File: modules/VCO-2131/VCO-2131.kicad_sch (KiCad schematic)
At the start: 51 parts, among them U4 SSI2131, U5 TL074, U6 TL074, U7 TL074, U8 CD4013

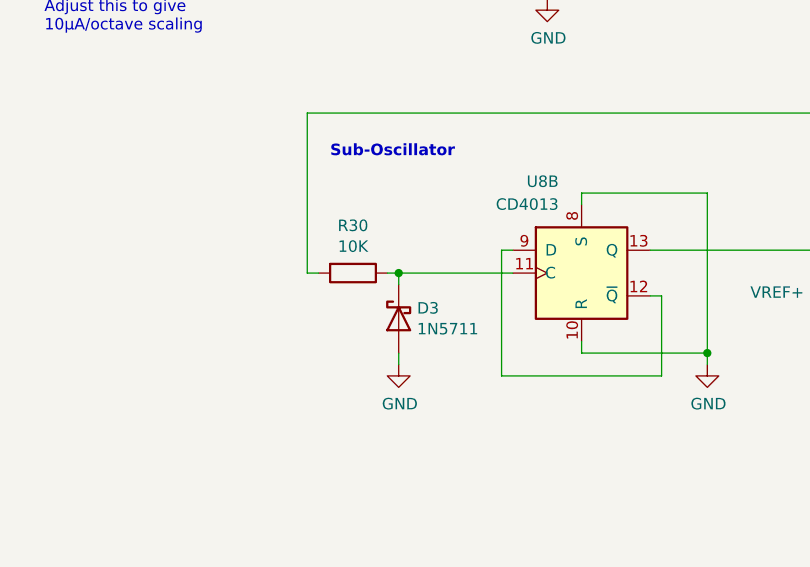
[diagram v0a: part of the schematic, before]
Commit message: VCO-2131: sub-oscillator fix
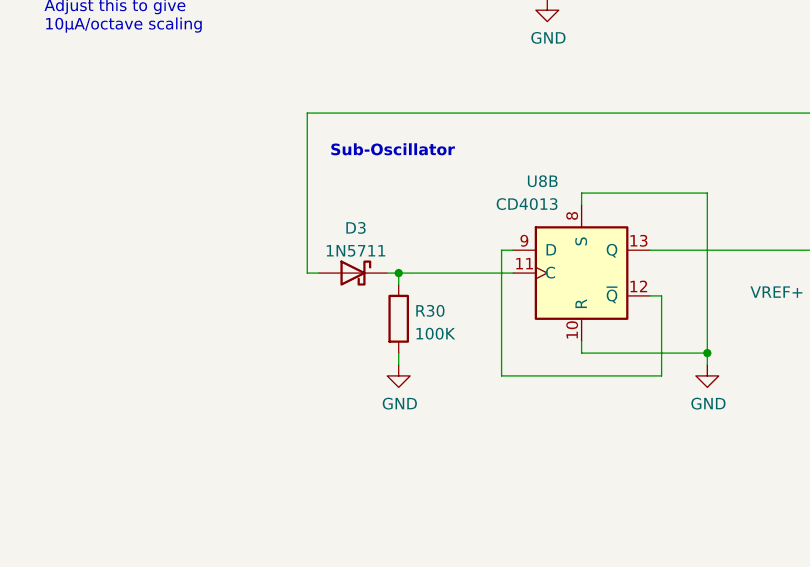
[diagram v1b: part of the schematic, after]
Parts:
- R30: value 10K -> 100K
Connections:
- net GND: now also R30.2; no longer D3.2 (A)
- net OUT-TRI: now also D3.2 (A); no longer R30.2
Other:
- moved on the sheet: D3, R30
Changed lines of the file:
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@@
   (title_block
     (title "Main - Eurorack SSI2131 VCO")
-    (date "2022-03-17")
-    (rev "1.3")
+    (date "2022-04-07")
+    (rev "1.4")
     (company "Len Popp")
     (comment 1 "Copyright © 2022 Len Popp CC BY")
@@
       (effects (font (size 1.27 1.27)) hide)
     )
+    (pin "1")
+    (pin "2")
+    (pin "3")
+    (pin "4")
+    (pin "5")
+    (pin "6")
     (pin "10")
     (pin "11")
@@
     (pin "8")
     (pin "9")
+    (pin "14")
+    (pin "7")
   )
   (symbol (lib_id "-lmp-synth:R_POT_TRIM_PCB_Vert_Bourns") (at 58.42 179.07 0) (mirror x) (unit 1)
@@
     (pin "2")
   )
-  (symbol (lib_name "R_1%_0W166_16") (lib_id "-lmp:R_1%_0W166") (at 156.21 137.16 270) (unit 1)
-    (in_bom yes) (on_board yes)
-    (property "Reference" "R30" (id 0) (at 156.21 131.9022 90))
-    (property "Value" "10K" (id 1) (at 156.21 134.2136 90))
-    (property "Footprint" "-lmp-misc:R_Axial_DIN0204_L3.6mm_D1.6mm_P7.62mm_Horizontal" (id 2) (at 156.21 135.382 90)
+  (symbol (lib_name "R_1%_0W166_16") (lib_id "-lmp:R_1%_0W166") (at 161.29 142.24 0) (unit 1)
+    (in_bom yes) (on_board yes) (fields_autoplaced)
+    (property "Reference" "R30" (id 0) (at 163.068 141.4053 0)
+      (effects (font (size 1.27 1.27)) (justify left))
+    )
+    (property "Value" "100K" (id 1) (at 163.068 143.9422 0)
+      (effects (font (size 1.27 1.27)) (justify left))
+    )
+    (property "Footprint" "-lmp-misc:R_Axial_DIN0204_L3.6mm_D1.6mm_P7.62mm_Horizontal" (id 2) (at 159.512 142.24 90)
       (effects (font (size 1.27 1.27)) hide)
     )
-    (property "Datasheet" "https://www.mouser.ca/datasheet/2/447/Yageo_LR_MFR_1-1714151.pdf" (id 3) (at 156.21 137.16 0)
+    (property "Datasheet" "https://www.mouser.ca/datasheet/2/447/Yageo_LR_MFR_1-1714151.pdf" (id 3) (at 161.29 142.24 0)
       (effects (font (size 1.27 1.27)) hide)
     )
-    (property "Value2" "1%, 1/6 W" (id 4) (at 156.21 141.478 90)
+    (property "Value2" "1%, 1/6 W" (id 4) (at 165.608 142.24 90)
       (effects (font (size 1.27 1.27)) hide)
     )
-    (property "Manufacturer" "YAGEO" (id 5) (at 156.21 137.16 0)
+    (property "Manufacturer" "YAGEO" (id 5) (at 161.29 142.24 0)
       (effects (font (size 1.27 1.27)) hide)
     )
-    (property "ManufacturerPartNum" "MFR-12FRF52-10K" (id 6) (at 156.21 137.16 0)
+    (property "ManufacturerPartNum" "MFR-12FRF52-10K" (id 6) (at 161.29 142.24 0)
       (effects (font (size 1.27 1.27)) hide)
     )
-    (property "Distributor" "Mouser" (id 7) (at 156.21 137.16 0)
+    (property "Distributor" "Mouser" (id 7) (at 161.29 142.24 0)
       (effects (font (size 1.27 1.27)) hide)
     )
-    (property "DistributorPartNum" "603-MFR-12FRF5210K" (id 8) (at 156.21 137.16 0)
+    (property "DistributorPartNum" "603-MFR-12FRF5210K" (id 8) (at 161.29 142.24 0)
       (effects (font (size 1.27 1.27)) hide)
     )
-    (property "DistributorPartLink" "https://www.mouser.ca/ProductDetail/YAGEO/MFR-12FRF52-10K?qs=%2Fha2pyFaduik%252B931GUVuOg6RLmmfil0yYFh5vxVUy4xd19JrveLWPw%3D%3D" (id 9) (at 156.21 137.16 0)
+    (property "DistributorPartLink" "https://www.mouser.ca/ProductDetail/YAGEO/MFR-12FRF52-10K?qs=%2Fha2pyFaduik%252B931GUVuOg6RLmmfil0yYFh5vxVUy4xd19JrveLWPw%3D%3D" (id 9) (at 161.29 142.24 0)
       (effects (font (size 1.27 1.27)) hide)
     )
@@
       (effects (font (size 1.27 1.27)) hide)
     )
+    (pin "1")
+    (pin "2")
+    (pin "3")
+    (pin "5")
+    (pin "6")
+    (pin "7")
     (pin "10")
     (pin "8")
     (pin "9")
+    (pin "12")
+    (pin "13")
+    (pin "14")
+    (pin "11")
+    (pin "4")
   )
   (symbol (lib_id "-lmp:CF") (at 153.67 57.15 90) (unit 1)
@@
       (effects (font (size 1.27 1.27)) hide)
     )
+    (pin "1")
+    (pin "2")
+    (pin "3")
+    (pin "5")
+    (pin "6")
+    (pin "7")
+    (pin "10")
+    (pin "8")
+    (pin "9")
     (pin "12")
     (pin "13")
     (pin "14")
+    (pin "11")
+    (pin "4")
   )
   (symbol (lib_name "R_1%_0W166_17") (lib_id "-lmp:R_1%_0W166") (at 214.63 68.58 270) (unit 1)
@@
       (effects (font (size 1.27 1.27)) hide)
     )
+    (pin "1")
+    (pin "2")
+    (pin "3")
+    (pin "5")
+    (pin "6")
+    (pin "7")
+    (pin "10")
+    (pin "8")
+    (pin "9")
     (pin "12")
     (pin "13")
     (pin "14")
+    (pin "11")
+    (pin "4")
   )
   (symbol (lib_id "-lmp-opamp:TL074") (at 91.44 39.37 0) (mirror x) (unit 4)
@@
       (effects (font (size 1.27 1.27)) hide)
     )
+    (pin "1")
+    (pin "2")
+    (pin "3")
+    (pin "5")
+    (pin "6")
+    (pin "7")
+    (pin "10")
+    (pin "8")
+    (pin "9")
     (pin "12")
     (pin "13")
     (pin "14")
+    (pin "11")
+    (pin "4")
   )
   (symbol (lib_name "R_1%_0W166_1") (lib_id "-lmp:R_1%_0W166") (at 72.39 36.83 270) (unit 1)
@@
       (effects (font (size 1.27 1.27)) hide)
     )
+    (pin "1")
+    (pin "2")
+    (pin "3")
     (pin "5")
     (pin "6")
     (pin "7")
+    (pin "10")
+    (pin "8")
+    (pin "9")
+    (pin "12")
+    (pin "13")
+    (pin "14")
+    (pin "11")
+    (pin "4")
   )
   (symbol (lib_name "R_1%_0W166_6") (lib_id "-lmp:R_1%_0W166") (at 83.82 130.81 270) (unit 1)
@@
     (pin "2")
     (pin "3")
+    (pin "5")
+    (pin "6")
+    (pin "7")
+    (pin "10")
+    (pin "8")
+    (pin "9")
+    (pin "12")
+    (pin "13")
+    (pin "14")
+    (pin "11")
+    (pin "4")
   )
   (symbol (lib_id "-lmp-opamp:TL074") (at 228.6 100.33 0) (mirror x) (unit 2)
@@
       (effects (font (size 1.27 1.27)) hide)
     )
+    (pin "1")
+    (pin "2")
+    (pin "3")
     (pin "5")
     (pin "6")
     (pin "7")
+    (pin "10")
+    (pin "8")
+    (pin "9")
+    (pin "12")
+    (pin "13")
+    (pin "14")
+    (pin "11")
+    (pin "4")
   )
   (symbol (lib_id "-lmp-opamp:TL074") (at 67.31 92.71 0) (mirror x) (unit 3)
@@
       (effects (font (size 1.27 1.27)) hide)
     )
+    (pin "1")
+    (pin "2")
+    (pin "3")
+    (pin "5")
+    (pin "6")
+    (pin "7")
     (pin "10")
     (pin "8")
     (pin "9")
+    (pin "12")
+    (pin "13")
+    (pin "14")
+    (pin "11")
+    (pin "4")
   )
   (symbol (lib_id "-lmp-opamp:TL074") (at 228.6 36.83 0) (mirror x) (unit 3)
@@
       (effects (font (size 1.27 1.27)) hide)
     )
+    (pin "1")
+    (pin "2")
+    (pin "3")
+    (pin "5")
+    (pin "6")
+    (pin "7")
     (pin "10")
     (pin "8")
     (pin "9")
+    (pin "12")
+    (pin "13")
+    (pin "14")
+    (pin "11")
+    (pin "4")
   )
   (symbol (lib_name "R_1%_0W166_18") (lib_id "-lmp:R_1%_0W166") (at 228.6 128.27 270) (unit 1)
@@
     (pin "2")
     (pin "3")
+    (pin "5")
+    (pin "6")
+    (pin "7")
+    (pin "10")
+    (pin "8")
+    (pin "9")
+    (pin "12")
+    (pin "13")
+    (pin "14")
+    (pin "11")
+    (pin "4")
   )
   (symbol (lib_id "-lmp-opamp:TL074") (at 67.31 130.81 0) (mirror x) (unit 2)
@@
       (effects (font (size 1.27 1.27)) hide)
     )
+    (pin "1")
+    (pin "2")
+    (pin "3")
     (pin "5")
     (pin "6")
     (pin "7")
+    (pin "10")
+    (pin "8")
+    (pin "9")
+    (pin "12")
+    (pin "13")
+    (pin "14")
+    (pin "11")
+    (pin "4")
   )
-  (symbol (lib_id "-lmp-diode:1N5711") (at 161.29 142.24 90) (mirror x) (unit 1)
-    (in_bom yes) (on_board yes)
-    (property "Reference" "D3" (id 0) (at 163.322 141.0716 90)
-      (effects (font (size 1.27 1.27)) (justify right))
-    )
-    (property "Value" "1N5711" (id 1) (at 163.322 143.383 90)
-      (effects (font (size 1.27 1.27)) (justify right))
-    )
-    (property "Footprint" "Diode_THT:D_DO-35_SOD27_P7.62mm_Horizontal" (id 2) (at 165.735 142.24 0)
+  (symbol (lib_id "-lmp-diode:1N5711") (at 156.21 137.16 0) (mirror y) (unit 1)
+    (in_bom yes) (on_board yes) (fields_autoplaced)
+    (property "Reference" "D3" (id 0) (at 156.5275 132.1902 0))
+    (property "Value" "1N5711" (id 1) (at 156.5275 134.7271 0))
+    (property "Footprint" "Diode_THT:D_DO-35_SOD27_P7.62mm_Horizontal" (id 2) (at 156.21 141.605 0)
       (effects (font (size 1.27 1.27)) hide)
     )
-    (property "Datasheet" "https://www.mouser.ca/datasheet/2/389/cd00000759-1795802.pdf" (id 3) (at 161.29 142.24 0)
+    (property "Datasheet" "https://www.mouser.ca/datasheet/2/389/cd00000759-1795802.pdf" (id 3) (at 156.21 137.16 0)
       (effects (font (size 1.27 1.27)) hide)
     )
-    (property "Manufacturer" "STMicroelectronics" (id 4) (at 161.29 142.24 0)
+    (property "Manufacturer" "STMicroelectronics" (id 4) (at 156.21 137.16 0)
       (effects (font (size 1.27 1.27)) hide)
     )
-    (property "ManufacturerPartNum" "1N5711" (id 5) (at 161.29 142.24 0)
+    (property "ManufacturerPartNum" "1N5711" (id 5) (at 156.21 137.16 0)
       (effects (font (size 1.27 1.27)) hide)
     )
-    (property "Distributor" "Mouser" (id 6) (at 161.29 142.24 0)
+    (property "Distributor" "Mouser" (id 6) (at 156.21 137.16 0)
       (effects (font (size 1.27 1.27)) hide)
     )
-    (property "DistributorPartNum" "511-1N5711" (id 7) (at 161.29 142.24 0)
+    (property "DistributorPartNum" "511-1N5711" (id 7) (at 156.21 137.16 0)
       (effects (font (size 1.27 1.27)) hide)
     )
-    (property "DistributorPartLink" "https://www.mouser.ca/ProductDetail/STMicroelectronics/1N5711?qs=FITO%2F%2FQgYDnH7pJ7rS2FRA%3D%3D" (id 8) (at 161.29 142.24 0)
+    (property "DistributorPartLink" "https://www.mouser.ca/ProductDetail/STMicroelectronics/1N5711?qs=FITO%2F%2FQgYDnH7pJ7rS2FRA%3D%3D" (id 8) (at 156.21 137.16 0)
       (effects (font (size 1.27 1.27)) hide)
     )
@@
     )
     (path "/00000000-0000-0000-0000-000061550c7d"
-      (reference "R30") (unit 1) (value "10K") (footprint "-lmp-misc:R_Axial_DIN0204_L3.6mm_D1.6mm_P7.62mm_Horizontal")
+      (reference "R30") (unit 1) (value "100K") (footprint "-lmp-misc:R_Axial_DIN0204_L3.6mm_D1.6mm_P7.62mm_Horizontal")
     )
     (path "/00000000-0000-0000-0000-000060e650d7"

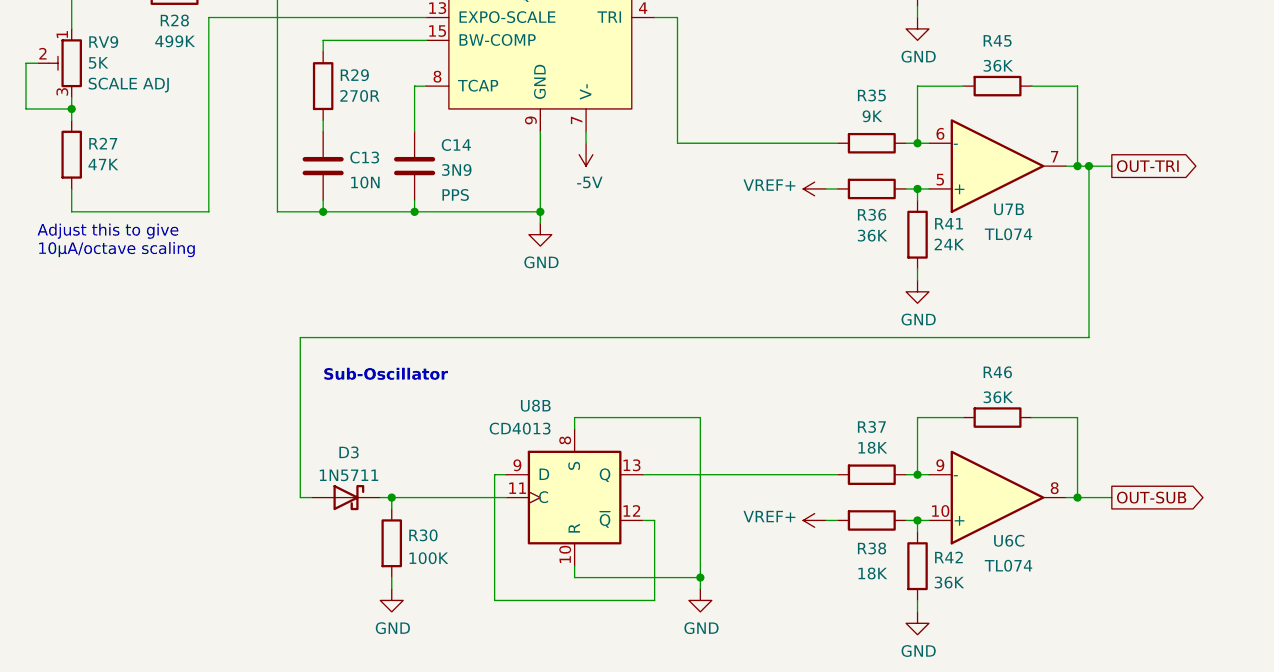
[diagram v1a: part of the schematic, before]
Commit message: VCO-2131: sub-oscillator fix
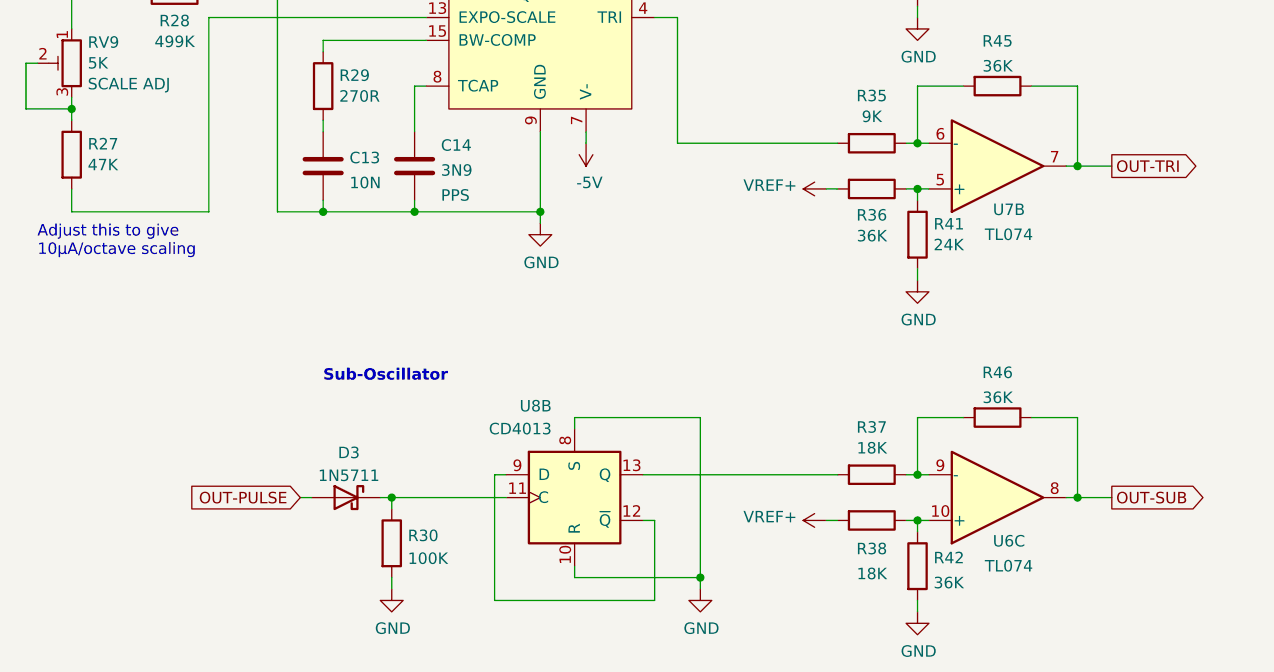
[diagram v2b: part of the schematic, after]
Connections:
- net OUT-PULSE: now also D3.2 (A)
- net OUT-TRI: no longer D3.2 (A)
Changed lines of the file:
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@@
   (junction (at 93.98 102.87) (diameter 0) (color 0 0 0 0)
   )
-  (junction (at 238.76 100.33) (diameter 0) (color 0 0 0 0)
-  )
   (junction (at 125.73 81.28) (diameter 0) (color 0 0 0 0)
   )
@@
     (stroke (width 0) (type default) (color 0 0 0 0))
   )
-  (wire (pts (xy 151.13 119.38) (xy 151.13 137.16))
-    (stroke (width 0) (type default) (color 0 0 0 0))
-  )
   (wire (pts (xy 195.58 128.27) (xy 195.58 146.05))
     (stroke (width 0) (type default) (color 0 0 0 0))
@@
     (stroke (width 0) (type default) (color 0 0 0 0))
   )
-  (wire (pts (xy 238.76 100.33) (xy 238.76 119.38))
-    (stroke (width 0) (type default) (color 0 0 0 0))
-  )
   (wire (pts (xy 219.71 60.96) (xy 219.71 68.58))
     (stroke (width 0) (type default) (color 0 0 0 0))
@@
     (stroke (width 0) (type default) (color 0 0 0 0))
   )
-  (wire (pts (xy 238.76 100.33) (xy 241.3 100.33))
+  (wire (pts (xy 237.49 100.33) (xy 241.3 100.33))
     (stroke (width 0) (type default) (color 0 0 0 0))
   )
@@
     (stroke (width 0) (type default) (color 0 0 0 0))
   )
-  (wire (pts (xy 151.13 119.38) (xy 238.76 119.38))
-    (stroke (width 0) (type default) (color 0 0 0 0))
-  )
   (wire (pts (xy 87.63 30.48) (xy 82.55 30.48))
     (stroke (width 0) (type default) (color 0 0 0 0))
@@
   )
   (wire (pts (xy 58.42 121.92) (xy 58.42 128.27))
-    (stroke (width 0) (type default) (color 0 0 0 0))
-  )
-  (wire (pts (xy 237.49 100.33) (xy 238.76 100.33))
     (stroke (width 0) (type default) (color 0 0 0 0))
   )
@@
     )
   )
+  (global_label "OUT-PULSE" (shape input) (at 151.13 137.16 180) (fields_autoplaced)
+    (effects (font (size 1.27 1.27)) (justify right))
+    (property "Intersheet References" "${INTERSHEET_REFS}" (id 0) (at 137.6177 137.0806 0)
+      (effects (font (size 1.27 1.27)) (justify right) hide)
+    )
+  )

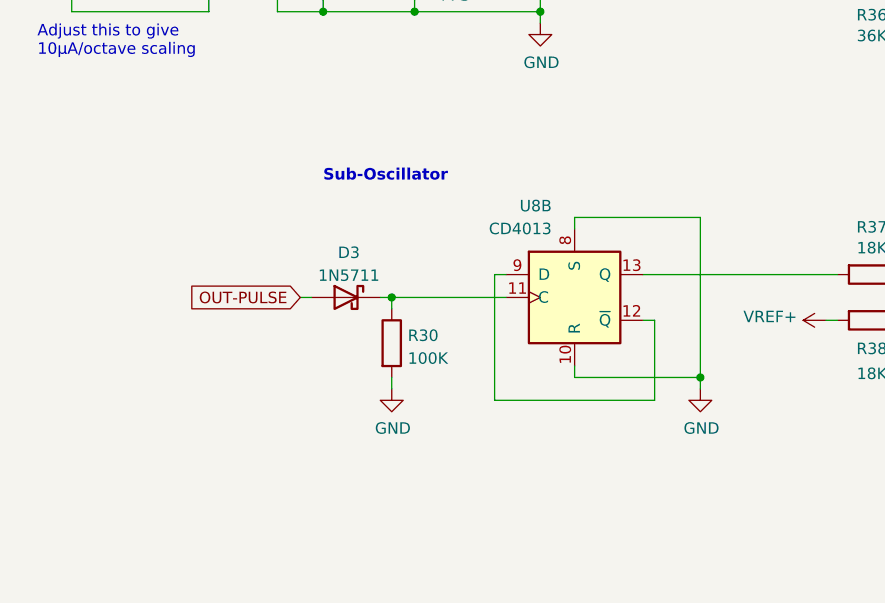
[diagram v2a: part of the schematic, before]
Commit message: VCO sub fix - update main module design (except gerbers)
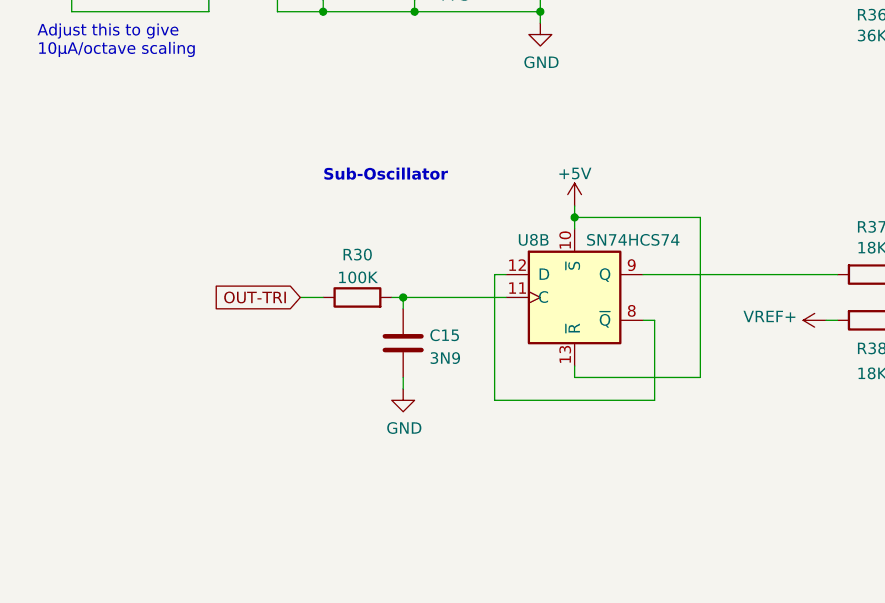
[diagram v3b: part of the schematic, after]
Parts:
- removed D3: 1N5711, Diode_THT:D_DO-35_SOD27_P7.62mm_Horizontal, symbol -lmp-diode:1N5711
- added C15: 3N9, -lmp-misc:C_Rect_Kemet_L7.2mm_W2.5mm_P5mm, symbol -lmp:CC
- R30: DistributorPartLink https://www.mouser.ca/ProductDetail/YAGEO/MFR-12FRF52-10K?q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 -> https://www.mouser.ca/ProductDetail/YAGEO/MFR-12FTF52-100K?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; DistributorPartNum 603-MFR-12FRF5210K -> 603-MFR-12FTF52-100K; ManufacturerPartNum MFR-12FRF52-10K -> MFR-12FTF52-100K
- U8: value CD4013 -> SN74HCS74; footprint Package_DIP:DIP-14_W7.62mm -> -lmp-breakout:Breakout_DIP-SOIC-14_W15.24mm; symbol -lmp-IC-misc:CD4013 -> -lmp-IC-misc:SN74HCS74; DistributorPartLink https://www.mouser.ca/ProductDetail/Texas-Instruments/CD401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 -> https://www.mouser.ca/ProductDetail/Texas-Instruments/SN74H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; DistributorPartNum 595-CD4013BE -> 595-SN74HCS74DR; ManufacturerPartNum CD4013BE -> SN74HCS74DR
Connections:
- net +5V: now also U8.10 (~{S}), U8.13 (~{R})
- net GND: now also C15.2; no longer R30.2, U8.10 (R), U8.8 (S)
- net OUT-TRI: now also R30.1
- net at R37.2: now also U8.9 (Q); no longer U8.13 (Q)
- net at U8.11 (C): now also R30.2, C15.1; no longer R30.1
- net at U8.12 (D): now also U8.8 (~{Q}); no longer U8.9 (D)
